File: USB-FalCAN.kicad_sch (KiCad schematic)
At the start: 59 parts, among them J1 Conn_01x17_Pin, J10 CAN, J2 NC, J3 Conn_01x17_Pin, J4 USB2.0_16P, J5 Boot, J6 NC, J7 DE9_Receptacle, J8 RS-485/422-TX, J9 RS-422-RX, SW3 BTN, U1 STM32F042C6Tx, U2 SN65HVD230, U3 SP3485EN, U4 SP3485EN, U5 MIC5504-3.3YM5, Y1 8MHz, Y2 32768Hz

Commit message: HarCAN
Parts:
- removed J7: DE9_Receptacle, Connector_Dsub:DSUB-9_Female_Horizontal_P2.77x2.84mm_EdgePinOffset7.70mm_Housed_MountingHolesOffset9.12mm, symbol Connector:DE9_Receptacle_MountingHoles
- removed J8: RS-485/422-TX, Connector_PinHeader_2.54mm:PinHeader_1x03_P2.54mm_Vertical, symbol Connector:Conn_01x03_Socket
- removed J9: RS-422-RX, Connector_PinHeader_2.54mm:PinHeader_1x03_P2.54mm_Vertical, symbol Connector:Conn_01x03_Socket
- removed R2: 10k, Resistor_SMD:R_0402_1005Metric, symbol Device:R
- removed U1: STM32F042C6Tx, Package_QFP:LQFP-48_7x7mm_P0.5mm, symbol MCU_ST_STM32F0:STM32F042C6Tx
- removed U2: SN65HVD230, Package_SO:SOIC-8_3.9x4.9mm_P1.27mm, symbol Interface_CAN_LIN:SN65HVD230
- added J11: G125-MH12005L1R, Harwin_Gecko:Harwin_G125-MH12005L1R_2x10_P1.25mm_Horizontal, symbol Harwin_Gecko:G125-MH12005L1R
- added U2: STM32G474CETx, Package_QFP:LQFP-48_7x7mm_P0.5mm, symbol MCU_ST_STM32G4:STM32G474CETx
- added U6: LTC2875-DD, Package_DFN_QFN:DFN-8-1EP_3x3mm_P0.5mm_EP1.66x2.38mm, symbol Interface_CAN_LIN:LTC2875-DD
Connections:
- net +3V3: now also U2.1 (VBAT), U2.20 (VREF+), U2.21 (VDDA), U2.24 (VDD), U2.36 (VDD), U2.48 (VDD), U6.3 (VCC); no longer J5.2 (Pin_2)
- net 422_DE: now also U2.17 (PB1)
- net 422_RE: now also U2.16 (PB0)
- net 485_DE: now also U2.29 (PB15)
- net 485_RE: now also U2.28 (PB14)
- net CAN_RX: now also R1.2, U2.45 (PB8), U6.4 (RXD)
- net CAN_TX: now also U2.46 (PB9), U6.1 (TXD)
- net D+: now also U2.34 (PA12)
- net D-: now also U2.33 (PA11)
- net GND: now also J11.15 (Pin_15), J11.19 (Pin_19), J11.3 (Pin_3), J11.7 (Pin_7), U2.19 (VSSA), U2.23 (VSS), U2.35 (VSS), U2.47 (VSS), U6.2 (GND), U6.9 (GND); no longer J5.6 (Pin_6)
- net I2C1_SCL: now also U2.22 (PB10)
- net I2C1_SDA: now also U2.25 (PB11)
- net PA0: now also U2.8 (PA0)
- net PA1: now also U2.9 (PA1)
- net PA10: now also U2.32 (PA10)
- net PA13: now also U2.37 (PA13)
- net PA14: now also U2.38 (PA14)
- net PA15: now also U2.39 (PA15)
- net PA2: now also U2.10 (PA2)
- net PA3: now also U2.11 (PA3)
- net PA4: now also U2.12 (PA4)
- net PA5: now also U2.13 (PA5)
- net PA6: now also U2.14 (PA6)
- net PA7: now also U2.15 (PA7)
- net PA8: now also U2.30 (PA8)
- net PA9: now also U2.31 (PA9)
- net PB12: now also U2.26 (PB12)
- net PB13: now also U2.27 (PB13)
- net PB2: now also U2.18 (PB2)
- net PB3: now also U2.40 (PB3)
- net PB4: now also U2.41 (PB4)
- net PB5: now also U2.42 (PB5)
- net PB6: now also U2.43 (PB6)
- net PB7: now also U2.44 (PB7)
- net PC13: now also U2.2 (PC13)
- net ~{NRST}: now also U2.7 (PG10)
- net at C3.1, Y1.1: now also U2.5 (PF0)
- net at TP1.1: now also U6.5 (SPLIT)
- net at R15.2, R16.1: now also U6.8 (RS)
- net 485_TX_H: now reaches R12.1, U3.6 (A)
- net 485_TX_H: now also J11.14 (Pin_14)
- net 485_TX_L: now reaches R12.2, U3.7 (B)
- net 485_TX_L: now also J11.16 (Pin_16)
- net 485_RX_H: now reaches R11.1, U4.6 (A)
- net 485_RX_H: now also J11.18 (Pin_18)
- net 485_RX_L: now reaches R11.2, U4.7 (B)
- net 485_RX_L: now also J11.20 (Pin_20)
- net at C2.1, Y1.3: now also U2.6 (PF1)
- net at C4.1, Y2.2: now also U2.3 (PC14)
- net at C7.1, Y2.1: now also U2.4 (PC15)
- net BOOT1: no longer names the net of J5.4 (Pin_4)
- net CAN_H renamed CAN1_H
- net CAN1_H: now also J11.2 (Pin_2), U6.7 (CANH)
- net CAN_L renamed CAN1_L
- net CAN1_L: now also J11.4 (Pin_4), U6.6 (CANL)
- new net CAN2_H: J11.6 (Pin_6)
- new net CAN2_L: J11.8 (Pin_8)
- new net CLOCK_H: J11.10 (Pin_10)
- new net CLOCK_L: J11.12 (Pin_12)
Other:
- moved on the sheet: C2, C3, FB1, J10, J2, J4, J6, R1, R10, R13, R14, R18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

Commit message: feat: more schematic
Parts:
- removed R18: 100k, Resistor_SMD:R_0402_1005Metric, symbol Device:R_Small
- J11: LCSC (none) -> C17484500
- U6: LCSC (none) -> C683035
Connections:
- net PB12 renamed CAN2_RX
- net PB13 renamed CAN2_TX
- net PB3 renamed CAN3_RX
- net PB4 renamed CAN3_TX
- no-connect marks 6 -> 2

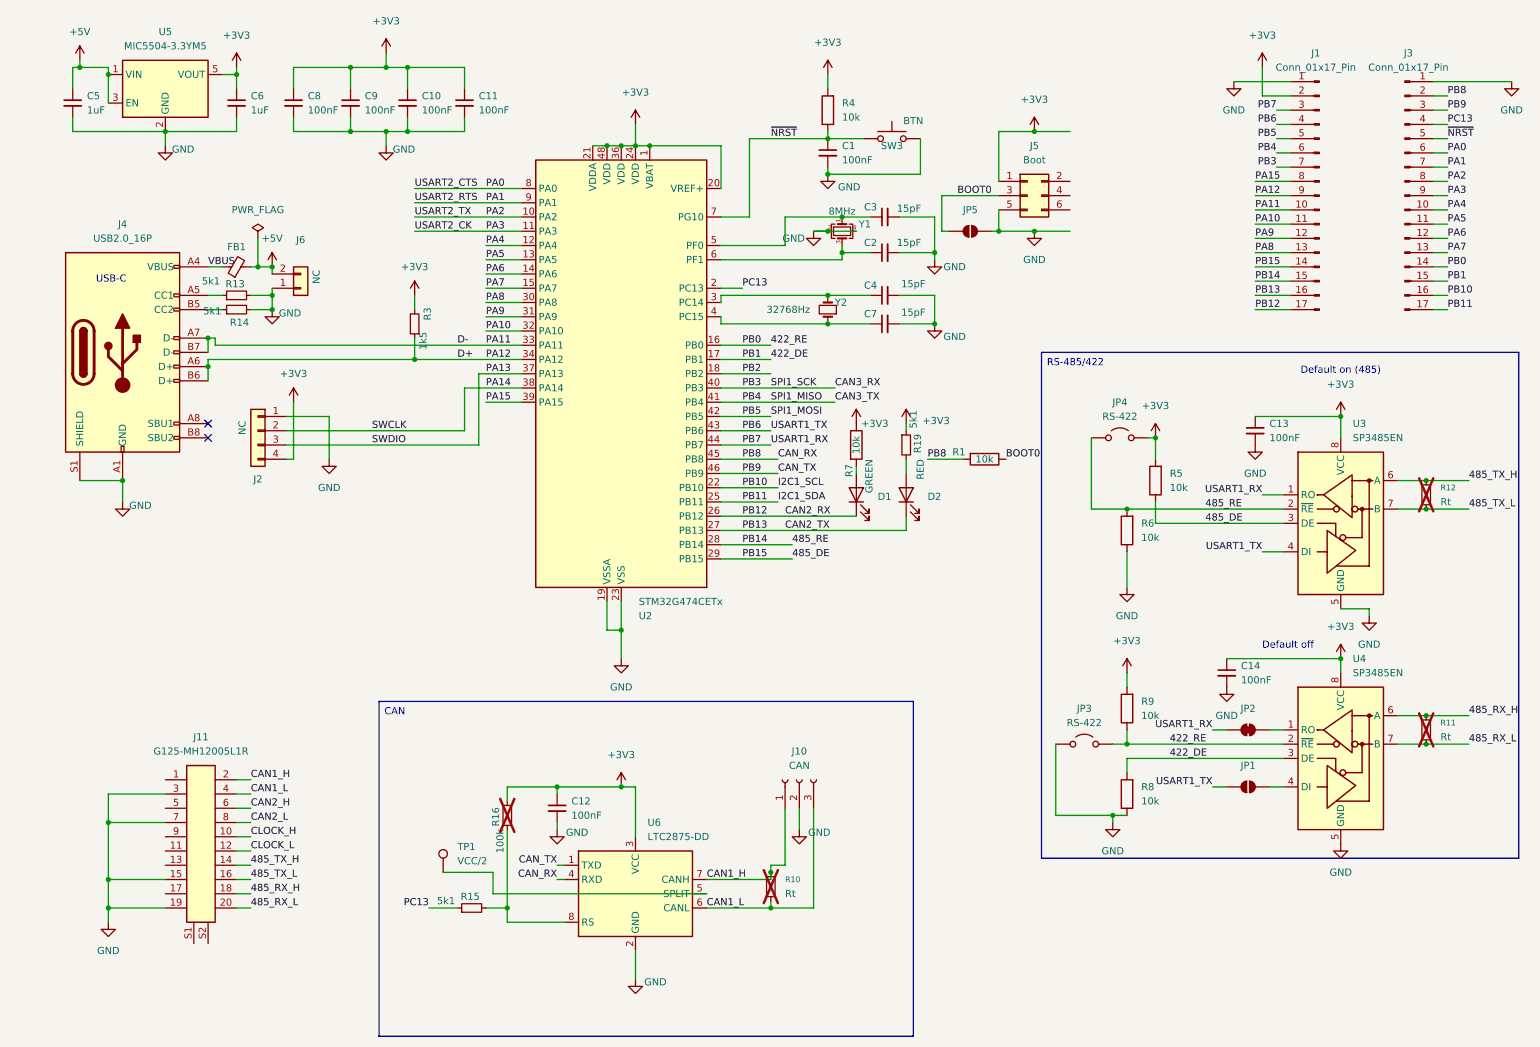
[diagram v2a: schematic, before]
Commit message: feat: rerouting started
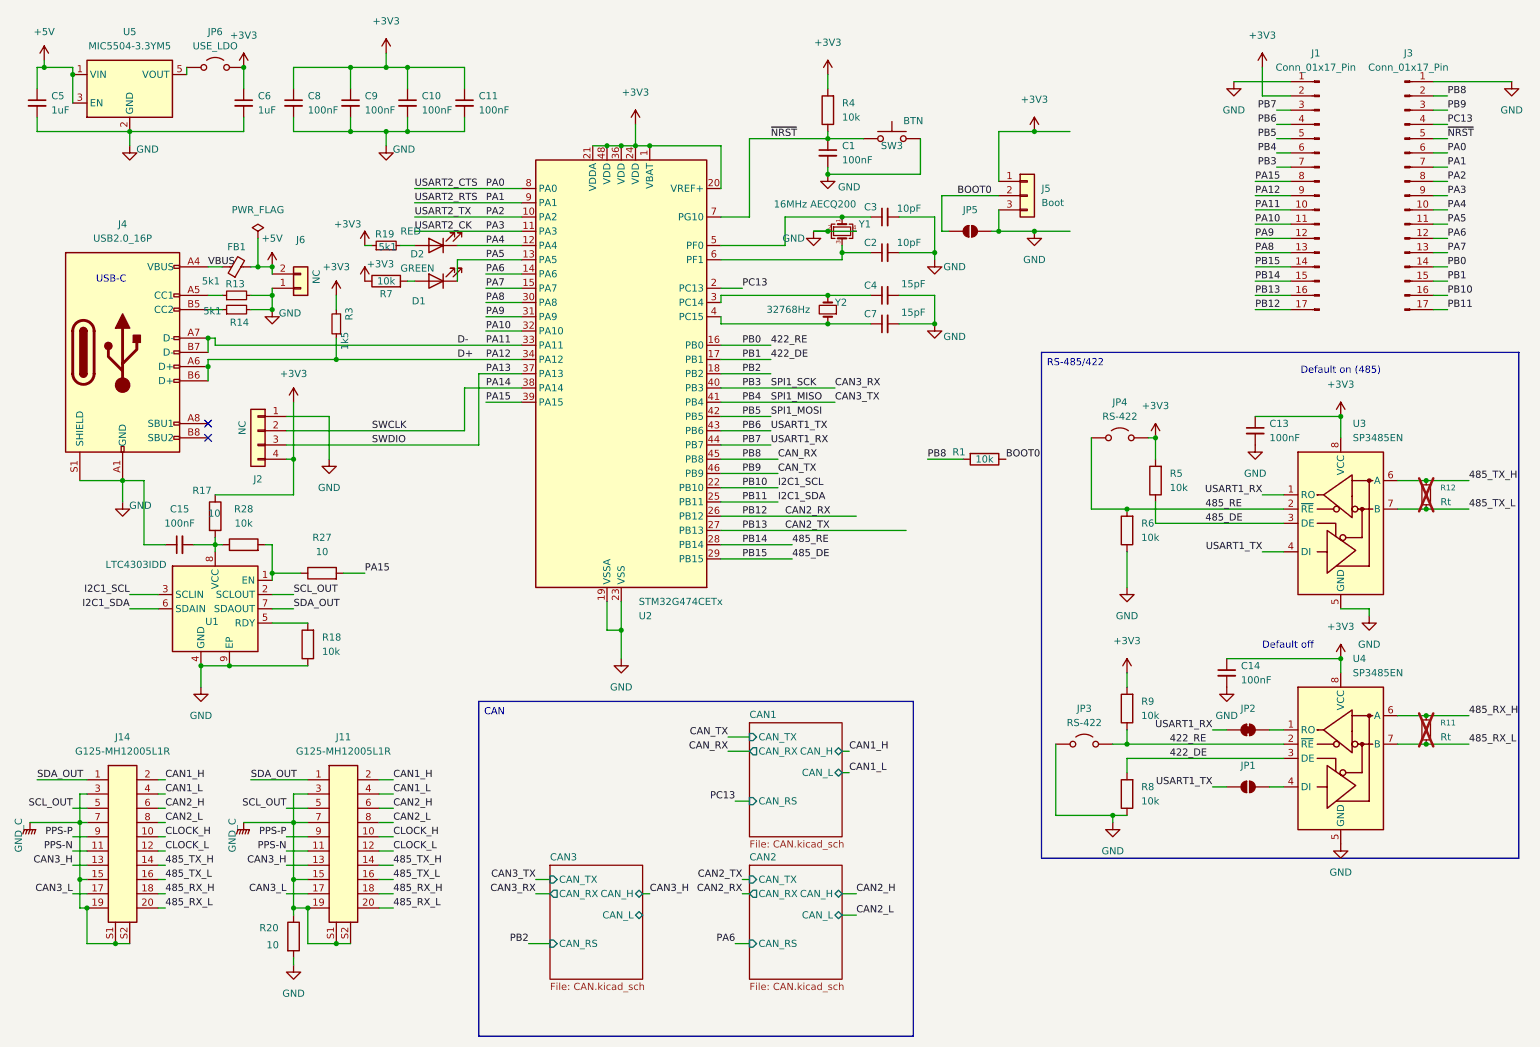
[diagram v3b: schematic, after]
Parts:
- removed C12: 100nF, Capacitor_SMD:C_0402_1005Metric, symbol Device:C_Small
- removed J10: CAN, Connector_PinHeader_2.54mm:PinHeader_1x03_P2.54mm_Vertical, symbol Connector:Conn_01x03_Socket
- removed R10: Rt, Resistor_SMD:R_0805_2012Metric, symbol Device:R_Small
- removed R15: 5k1, Resistor_SMD:R_0402_1005Metric, symbol Device:R_Small
- removed R16: 100k, Resistor_SMD:R_0402_1005Metric, symbol Device:R_Small
- removed TP1: VCC/2, TestPoint:TestPoint_Pad_D1.0mm, symbol Connector:TestPoint
- removed U6: LTC2875-DD, Package_DFN_QFN:DFN-8-1EP_3x3mm_P0.5mm_EP1.66x2.38mm, symbol Interface_CAN_LIN:LTC2875-DD
- added C15: 100nF, Capacitor_SMD:C_0402_1005Metric, symbol Device:C_Small
- added J14: G125-MH12005L1R, Harwin_Gecko:Harwin_G125-MH12005L1R_2x10_P1.25mm_Horizontal, symbol Harwin_Gecko:G125-MH12005L1R
- added JP6: USE_LDO, Connector_PinHeader_2.54mm:PinHeader_1x02_P2.54mm_Vertical, symbol Jumper:Jumper_2_Open
- added R17, R20, R27: 10, Resistor_SMD:R_0402_1005Metric, symbol Device:R
- added R18, R28: 10k, Resistor_SMD:R_0402_1005Metric, symbol Device:R
- added U1: LTC4303IDD, Package_DFN_QFN:DFN-8-1EP_3x3mm_P0.5mm_EP1.66x2.38mm, symbol LTC4303:LTC4303IDD
- C2, C3: value 15pF -> 10pF
- J5: footprint Connector_PinHeader_2.54mm:PinHeader_2x03_P2.54mm_Vertical -> Connector_PinHeader_2.54mm:PinHeader_1x03_P2.54mm_Vertical; symbol Connector_Generic:Conn_02x03_Odd_Even -> Connector_Generic:Conn_01x03
- Y1: value 8MHz -> 16MHz AECQ200
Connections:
- net +3V3: now also JP6.2 (B), R17.1; no longer U5.5 (VOUT)
- net 485_RX_H: now also J14.18 (Pin_18)
- net 485_RX_L: now also J14.20 (Pin_20)
- net 485_TX_H: now also J14.14 (Pin_14)
- net 485_TX_L: now also J14.16 (Pin_16)
- net BOOT0: now also J5.2 (Pin_2); no longer J5.3 (Pin_3)
- net CAN1_H: now also J14.2 (Pin_2)
- net CAN1_L: now also J14.4 (Pin_4)
- net CAN2_H: now also J14.6 (Pin_6)
- net CAN2_L: now also J14.8 (Pin_8)
- net CAN2_RX: no longer D1.1 (K)
- net CAN2_TX: no longer D2.1 (K)
- net CLOCK_H: now also J14.10 (Pin_10)
- net CLOCK_L: now also J14.12 (Pin_12)
- net GND: now also J5.3 (Pin_3), C15.1, R18.1, R20.2, U1.4 (GND), U1.9 (EP); no longer J11.15 (Pin_15), J11.19 (Pin_19), J11.3 (Pin_3), J11.7 (Pin_7), J5.5 (Pin_5)
- net I2C1_SCL: now also U1.3 (SCLIN)
- net I2C1_SDA: now also U1.6 (SDAIN)
- net PA15: now also R27.2
- net PA4: now also D2.1 (K)
- net PA5: now also D1.1 (K)
- net SDA_OUT: now reaches J11.1 (Pin_1)
- net SDA_OUT: now also J14.1 (Pin_1), U1.7 (SDAOUT)
- net PPS-N: now reaches J11.11 (Pin_11)
- net PPS-N: now also J14.11 (Pin_11)
- net CAN3_H: now reaches J11.13 (Pin_13)
- net CAN3_H: now also J14.13 (Pin_13)
- net CAN3_L: now reaches J11.17 (Pin_17)
- net CAN3_L: now also J14.17 (Pin_17)
- net SCL_OUT: now reaches J11.5 (Pin_5)
- net SCL_OUT: now also J14.5 (Pin_5), U1.2 (SCLOUT)
- net PPS-P: now reaches J11.9 (Pin_9)
- net PPS-P: now also J14.9 (Pin_9)
- net GND_C: now reaches J11.S1 (MP)
- net GND_C: now also J11.15 (Pin_15), J11.19 (Pin_19), J11.3 (Pin_3), J11.7 (Pin_7), J11.S2 (MP), J14.15 (Pin_15), J14.19 (Pin_19), J14.3 (Pin_3), J14.7 (Pin_7), J14.S1 (MP), J14.S2 (MP), R20.1
- new net: C15.2, R17.2, R28.1, U1.8 (VCC)
- new net: JP6.1 (A), U5.5 (VOUT)
- new net: R27.1, R28.2, U1.1 (EN)
- new net: R18.2, U1.5 (RDY)
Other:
- added sheet CAN1 (CAN.kicad_sch)
- added sheet CAN2 (CAN.kicad_sch)
- added sheet CAN3 (CAN.kicad_sch)
- moved on the sheet: C5, C6, D1, D2, J11, R19, R3, R7, U5

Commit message: feat: more routing
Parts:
- removed JP6: USE_LDO, Connector_PinHeader_2.54mm:PinHeader_1x02_P2.54mm_Vertical, symbol Jumper:Jumper_2_Open
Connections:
- net +3V3: no longer C6.1
- net PA15: no longer R27.2
- net PA4: no longer D2.1 (K)
- net PA5: no longer D1.1 (K)
- net PA7: now also R27.2
- net PA8: now also D1.1 (K)
- net PA9: now also D2.1 (K)
- net PB7: no longer J1.3 (Pin_3)
- net LDO_VOUT: now reaches U5.5 (VOUT)
- net LDO_VOUT: now also C6.1, J1.3 (Pin_3)
- net 485_RX_H renamed 485_RX_P
- net 485_RX_L renamed 485_RX_N
- net 485_TX_H renamed 485_TX_P
- net 485_TX_L renamed 485_TX_N
- net CLOCK_H renamed CLOCK-P
- net CLOCK_L renamed CLOCK-N

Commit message: feat: Harwin main connectors
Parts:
- added C18: 1uF, Capacitor_SMD:C_0805_2012Metric, symbol Device:C_Small
- added R2: 100k, Resistor_SMD:R_0402_1005Metric, symbol Device:R
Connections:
- net +3V3: now also C18.1
- net BOOT0: now also R2.1
- net GND: now also C18.2, R2.2
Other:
- moved on the sheet: R1

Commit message: fix: JLC part numbers
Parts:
- Y1: LCSC C5308002 -> C13738
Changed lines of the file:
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@@
 			)
 		)
-		(property "LCSC" "C5308002"
+		(property "LCSC" "C13738"
 			(at 163.83 53.34 0)
 			(hide yes)
